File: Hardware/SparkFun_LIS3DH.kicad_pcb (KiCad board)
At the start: 2 copper layers, 25.4 x 25.4 mm, 43 parts, among them J3 Qwiic_RA, J4 I2C, J5 Qwiic_RA, U1 VEML7700-TT

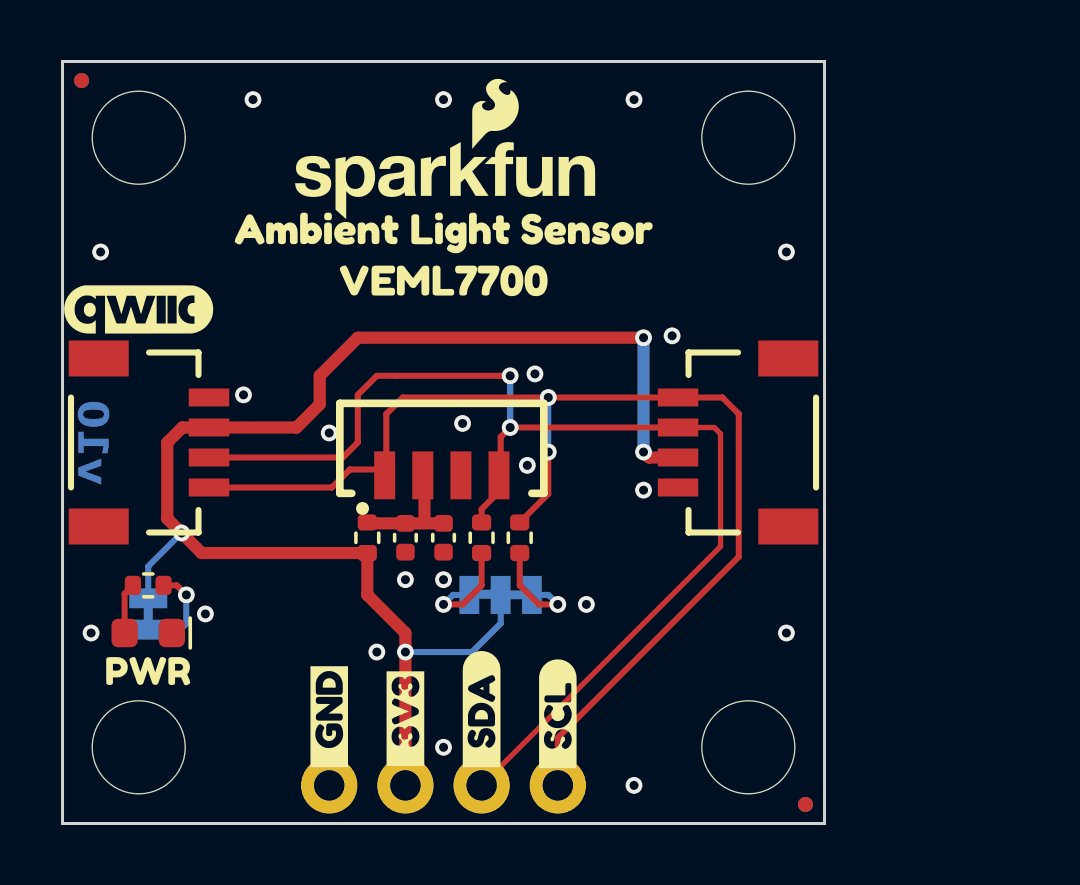
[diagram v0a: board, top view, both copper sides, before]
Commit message: Adds the new LIS3DH symbol and footprint to schematic and PCB
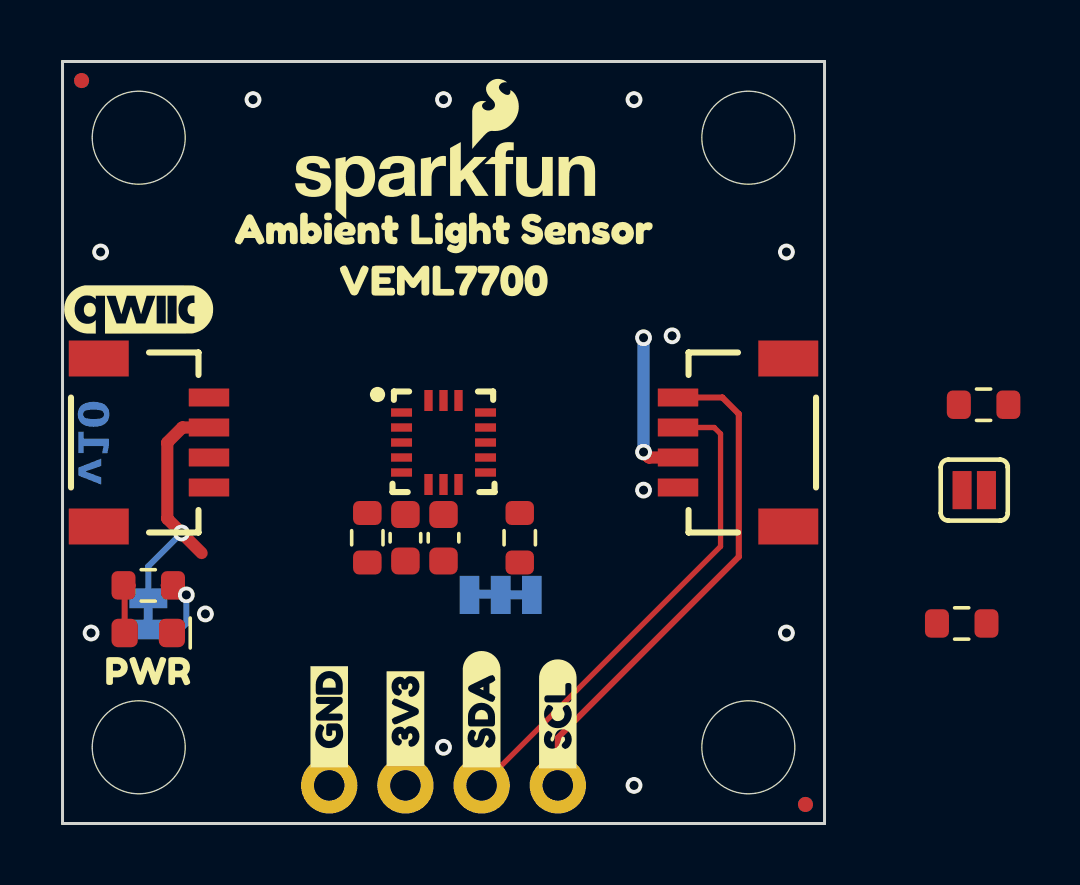
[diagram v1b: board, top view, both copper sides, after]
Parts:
- removed R6: 2.2k, SparkFun-Resistor:R_0402_1005Metric
- added JP3: ADDR, SparkFun-Jumper:Jumper_2_NO, F.Cu at (153.7, 99.7)
- added R4: 10k, SparkFun-Resistor:R_0603_1608Metric, F.Cu at (154.0, 96.8)
- added R5: 4.7k, SparkFun-Resistor:R_0603_1608Metric, F.Cu at (153.2, 104.1)
- C1: value 2.2uF -> 10uF; footprint SparkFun-Capacitor:C_0402_1005Metric -> SparkFun-Capacitor:C_0603_1608Metric
- C2: footprint SparkFun-Capacitor:C_0402_1005Metric -> SparkFun-Capacitor:C_0603_1608Metric
- R1: value 4.7 -> 10k; footprint SparkFun-Resistor:R_0402_1005Metric -> SparkFun-Resistor:R_0603_1608Metric
- R2: footprint SparkFun-Resistor:R_0402_1005Metric -> SparkFun-Resistor:R_0603_1608Metric
- R3: value 4.7k -> 2.2k; footprint SparkFun-Resistor:R_0402_1005Metric -> SparkFun-Resistor:R_0603_1608Metric
- U1: value VEML7700-TT -> LIS3DH; footprint SparkFun-Sensor:VEML7700-TT -> SparkFun-Sensor:LGA-16-3X3
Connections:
- C1 pad 1: Net-(U1-VDD) -> 3.3V
- C2 pad 1: Net-(U1-VDD) -> 3.3V
- R1 pad 1: Net-(U1-VDD) -> ~{CS}
- R2 pad 1: SCL -> SDA
- R2 pad 2: Net-(JP2-A) -> Net-(JP2-C)
- R3 pad 1: Net-(D1-A) -> SCL
- R3 pad 2: Net-(JP1-A) -> Net-(JP2-A)
- U1 pad 1: SCL -> 3.3V
- U1 pad 2: Net-(U1-VDD) -> (no net)
- U1 pad 3: GND -> (no net)
- U1 pad 4: SDA -> SCL
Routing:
- net 3.3V: track 48.2 -> 13.4 mm, vias 4 -> 3
- net SDA: track 39.6 -> 16.4 mm, vias 2 -> 0
- net SCL: track 39.8 -> 17.0 mm, vias 2 -> 0
- net Net-(U1-VDD): track 4.19 -> 0.00 mm
- net Net-(JP2-A): track 3.61 -> 0.00 mm, vias 1 -> 0
- net Net-(JP2-C): track 3.61 -> 0.00 mm, vias 1 -> 0
- net GND: vias 21 -> 12

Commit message: Adds silks, moves components arounds
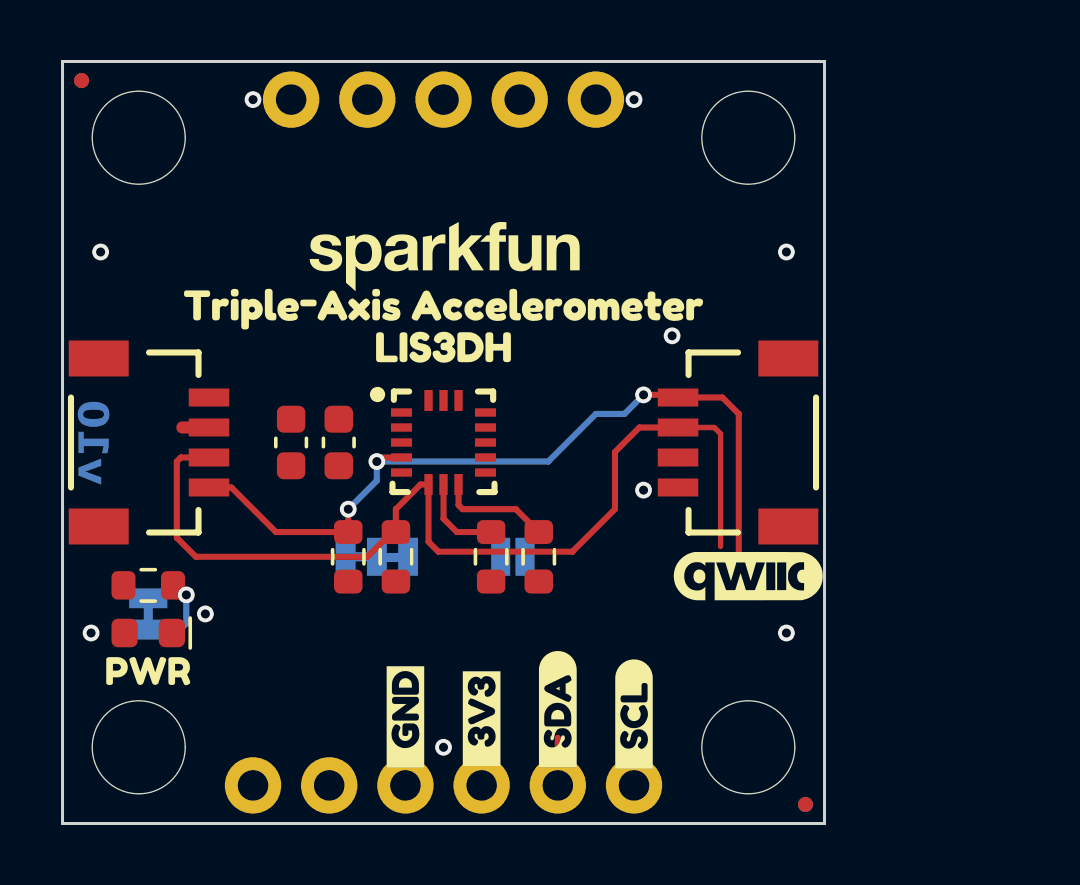
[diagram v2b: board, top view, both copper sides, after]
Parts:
- removed the G*** at (136.0, 89.2) (x2)
- removed kibuzzard-680A7834 (x2): G***, kibuzzard-680A7834
- removed kibuzzard-680A784B (x2): G***, kibuzzard-680A784B
- removed kibuzzard-680BA25F: G***, kibuzzard-680BA25F
- added G***: LOGO, SparkFun-Aesthetic:SparkFun_Logo_NoFlame_9mm, F.Cu at (136.0, 91.8)
- added G***: LOGO, SparkFun-Aesthetic:SparkFun_Logo_NoFlame_9mm, B.Cu at (136.0, 91.8)
- added J1: Conn_01x02, SparkFun-Connector:1x02, F.Cu at (129.6, 109.5)
- added J2: Conn_01x05, SparkFun-Connector:1x05, F.Cu at (141.0, 86.7)
- added kibuzzard-68376F48: G***, kibuzzard-68376F48, F.Cu at (136.0, 94.9)
- added kibuzzard-68376F54: G***, kibuzzard-68376F54, F.Cu at (136.0, 93.7)
- added kibuzzard-68377305: G***, kibuzzard-68377305, B.Cu at (136.0, 95.2)
- added kibuzzard-68377311: G***, kibuzzard-68377311, B.Cu at (136.0, 96.8)
- added kibuzzard-6837731A: G***, kibuzzard-6837731A, B.Cu at (136.0, 98.1)
- JP3: moved to B.Cu
- moved R5 27.1 mm to (126.1, 102.9)
- moved G*** 22.2 mm to (146.1, 102.6) (x2)
- moved R4 17.2 mm to (137.6, 101.9), turned to -90 degrees
- moved JP3 15.5 mm to (138.3, 101.9), turned to 180 degrees
- moved Ref** 10.6 mm to (147.4, 93.3)
- moved R3 6.74 mm to (132.8, 101.9), turned to -90 degrees
- moved C2 5.99 mm to (130.9, 98.1)
- moved R1 5.75 mm to (139.1, 101.9)
- moved kibuzzard-67D9D97F 4.44 mm to (130.6, 101.9)
- moved JP2 4.32 mm to (133.7, 101.9), turned to 0 degrees
- moved R2 4.18 mm to (134.4, 101.9)
- moved C1 3.88 mm to (132.5, 98.1)
- moved kibuzzard-67BF7CFE 2.54 mm to (139.8, 107.0)
- moved kibuzzard-67BF7F13 2.54 mm to (139.8, 107.0)
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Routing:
- net SDA: track 16.4 -> 33.7 mm
- net 3.3V: track 13.4 -> 0.77 mm, vias 3 -> 0
- net SCL: track 17.0 -> 26.8 mm, vias 0 -> 3
- net ~{CS}: track 0.00 -> 3.73 mm
- net ADDR/SDO: track 0.00 -> 2.91 mm
- net Net-(D1-A): track 1.70 -> 0.00 mm
- net Net-(JP1-A): track 3.20 -> 2.31 mm

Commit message: Adds silk to top
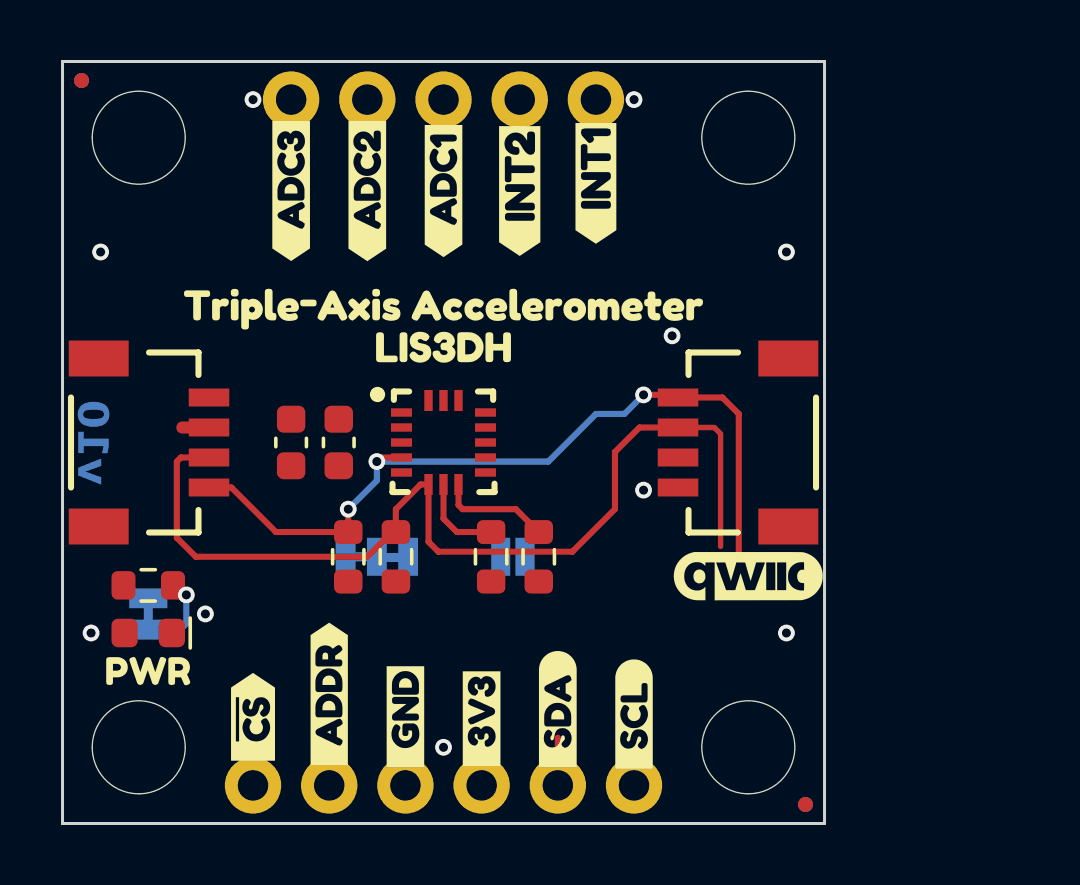
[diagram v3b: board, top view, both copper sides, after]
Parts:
- removed the G*** at (136.0, 91.8)
- added kibuzzard-6838798C: G***, kibuzzard-6838798C, F.Cu at (141.0, 89.5)
- added kibuzzard-683879AC: G***, kibuzzard-683879AC, F.Cu at (138.5, 89.7)
- added kibuzzard-68387A29: G***, kibuzzard-68387A29, F.Cu at (136.0, 89.7)
- added kibuzzard-68387A37: G***, kibuzzard-68387A37, F.Cu at (133.4, 89.7)
- added kibuzzard-68387A3F: G***, kibuzzard-68387A3F, F.Cu at (130.9, 89.7)
- added kibuzzard-68387A66: G***, kibuzzard-68387A66, F.Cu at (129.6, 107.2)
- added kibuzzard-68387A76: G***, kibuzzard-68387A76, F.Cu at (132.2, 106.5)

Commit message: Adjust routing, adds keepout underneath sensor, moves clock out from underneath IC
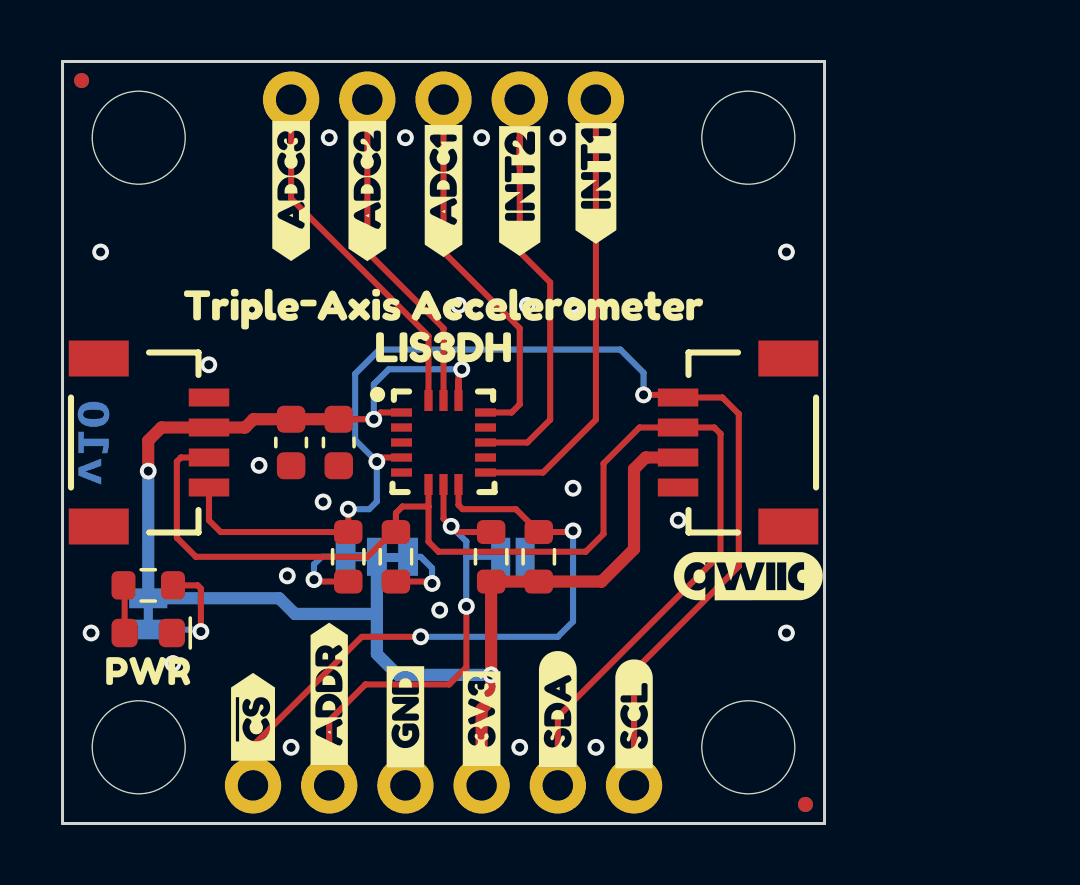
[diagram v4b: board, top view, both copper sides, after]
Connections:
- J2 pad 1: INT1 -> INT2
- J2 pad 2: INT2 -> INT1
- J2 pad 3: ADC1 -> ADC3
- J2 pad 5: ADC3 -> ADC1
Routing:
- net 3.3V: track 0.77 -> 51.6 mm, vias 0 -> 4
- net ~{CS}: track 3.73 -> 21.6 mm, vias 0 -> 2
- net INT2: track 0.00 -> 15.1 mm
- net INT1: track 0.00 -> 14.6 mm
- net SCL: track 26.8 -> 41.3 mm
- net ADDR/SDO: track 2.91 -> 16.4 mm, vias 0 -> 2
- net ADC3: track 0.00 -> 12.5 mm
- net ADC1: track 0.00 -> 11.9 mm
- net ADC2: track 0.00 -> 11.1 mm
- net SDA: track 33.7 -> 42.2 mm
- net Net-(JP2-A): track 0.00 -> 2.84 mm, vias 0 -> 1
- net Net-(JP2-C): track 0.00 -> 2.70 mm, vias 0 -> 1
- net Net-(JP1-A): track 2.31 -> 4.19 mm
- net Net-(D1-A): track 0.00 -> 1.60 mm
- net GND: vias 12 -> 22
